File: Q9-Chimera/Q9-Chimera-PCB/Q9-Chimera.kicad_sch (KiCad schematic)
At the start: 199 parts, among them J1 Conn_01x07, J2 USB_C_Receptacle_USB2.0_16P, J3 Conn_01x05, SW1 RotaryEncoder_Switch, SW2 RotaryEncoder_Switch, U1 XC6206PxxxMR, U2 SRV05-4, U3 RP2040, U4 W25Q128JVS, Y1 Crystal_GND24

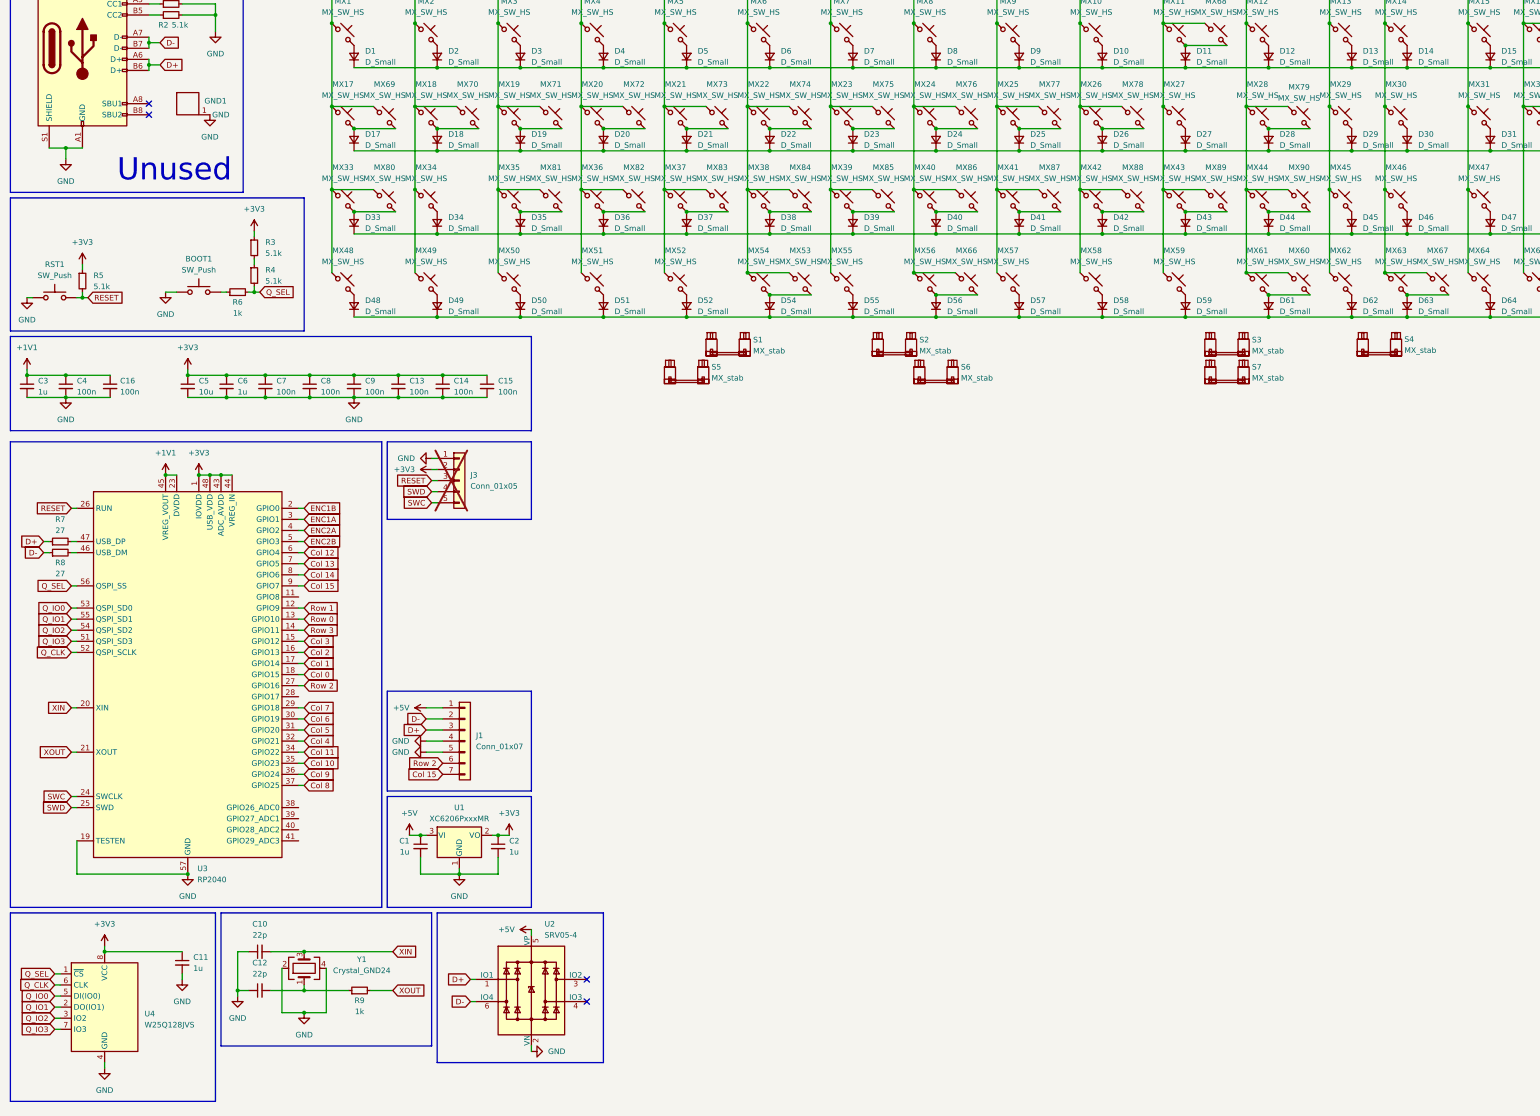
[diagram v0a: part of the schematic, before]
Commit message: complete addition of 225/275 bars and associated tweaks
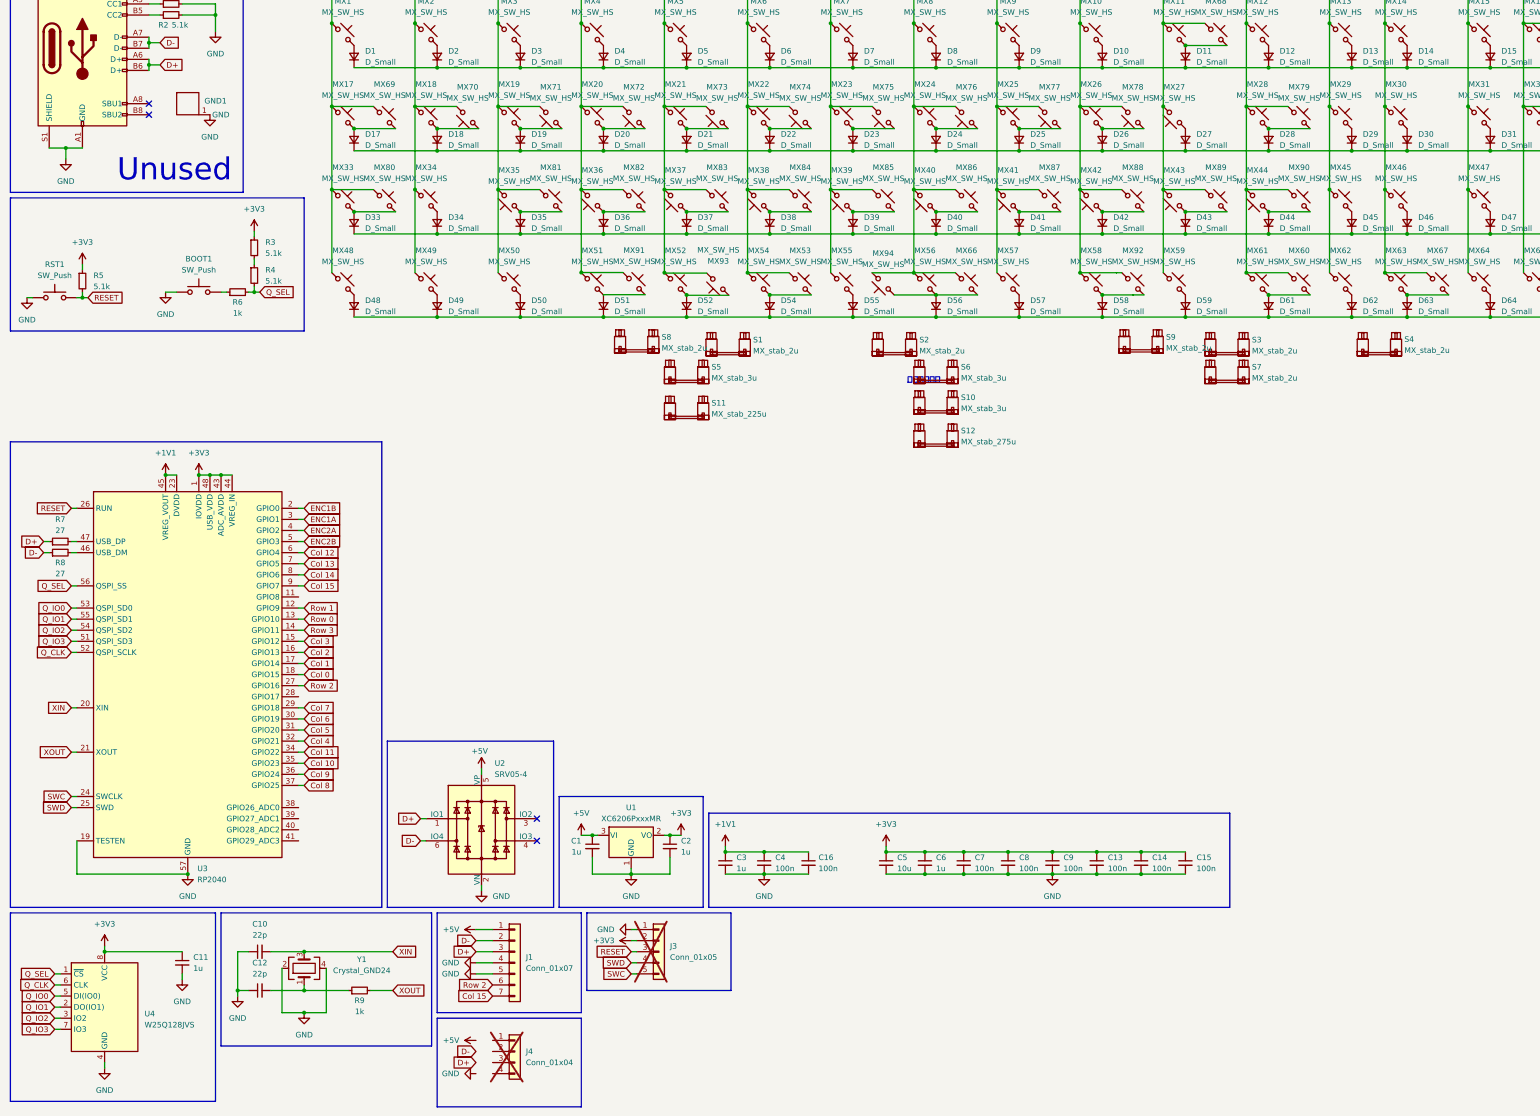
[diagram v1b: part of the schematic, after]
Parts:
- added J4: Conn_01x04, symbol Connector_Generic:Conn_01x04
- added MX91, MX92: MX_SW_HS, PCM_marbastlib-mx:SW_MX_HS_CPG151101S11_1u, symbol PCM_marbastlib-mx:MX_SW_HS_CPG151101S11
- added MX93, MX94: MX_SW_HS, PCM_marbastlib-mx:SW_MX_1u, symbol PCM_marbastlib-mx:MX_SW_HS_CPG151101S11
- added S10: MX_stab_3u, PCM_marbastlib-mx:STAB_MX_3u, symbol PCM_marbastlib-mx:MX_stab
- added S11: MX_stab_225u, PCM_marbastlib-mx:STAB_MX_2.25u, symbol PCM_marbastlib-mx:MX_stab
- added S12: MX_stab_275u, PCM_marbastlib-mx:STAB_MX_2.75u, symbol PCM_marbastlib-mx:MX_stab
- added S8, S9: MX_stab_2u, PCM_marbastlib-mx:STAB_MX_2u, symbol PCM_marbastlib-mx:MX_stab
- MX53: footprint PCM_marbastlib-mx:SW_MX_HS_CPG151101S11_1u -> PCM_marbastlib-mx:SW_MX_1u
- S1, S2, S3, S4, S7: value MX_stab -> MX_stab_2u
- S5, S6: value MX_stab -> MX_stab_3u
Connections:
- net Col 1: now also MX70.2; no longer MX70.1
- net Col 10: now also MX27.2, MX43.2; no longer MX27.1, MX43.1
- net Col 11: now also MX44.2; no longer MX44.1
- net Col 2: now also MX35.2, MX71.2; no longer MX35.1, MX71.1
- net Col 3: now also MX36.2, MX72.2, MX91.1; no longer MX36.1, MX72.1
- net Col 4: now also MX37.2, MX73.2, MX93.2; no longer MX37.1, MX73.1
- net Col 5: now also MX38.2, MX74.2; no longer MX38.1, MX74.1
- net Col 6: now also MX39.2, MX75.2; no longer MX39.1, MX75.1
- net Col 7: now also MX40.2, MX76.2, MX94.2; no longer MX40.1, MX76.1
- net Col 8: now also MX41.2, MX77.2; no longer MX41.1, MX77.1
- net Col 9: now also MX42.2, MX78.2, MX92.1; no longer MX42.1, MX78.1
- net at D39.2 (A), MX85.2: now also MX39.1; no longer MX39.2
- net at D24.2 (A), MX24.2: now also MX76.1; no longer MX76.2
- net at D21.2 (A), MX21.2: now also MX73.1; no longer MX73.2
- net at D40.2 (A), MX86.2: now also MX40.1; no longer MX40.2
- net at D35.2 (A), MX81.2: now also MX35.1; no longer MX35.2
- net at D41.2 (A), MX87.2: now also MX41.1; no longer MX41.2
- net at D20.2 (A), MX20.2: now also MX72.1; no longer MX72.2
- net at D37.2 (A), MX83.2: now also MX37.1; no longer MX37.2
- net at D27.2 (A): now also MX27.1; no longer MX27.2
- net at D22.2 (A), MX22.2: now also MX74.1; no longer MX74.2
- net at D42.2 (A), MX88.2: now also MX42.1; no longer MX42.2
- net at D23.2 (A), MX23.2: now also MX75.1; no longer MX75.2
- net at D18.2 (A), MX18.2: now also MX70.1; no longer MX70.2
- net at D43.2 (A), MX89.2: now also MX43.1; no longer MX43.2
- net at D25.2 (A), MX25.2: now also MX77.1; no longer MX77.2
- net at D58.2 (A), MX58.2: now also MX92.2
- net at D56.2 (A), MX56.2, MX66.2: now also MX94.1
- net at D52.2 (A), MX52.2: now also MX93.1
- net at D51.2 (A), MX51.2: now also MX91.2
- net at D26.2 (A), MX26.2: now also MX78.1; no longer MX78.2
- net at D36.2 (A), MX82.2: now also MX36.1; no longer MX36.2
- net at D44.2 (A), MX90.2: now also MX44.1; no longer MX44.2
- net at D19.2 (A), MX19.2: now also MX71.1; no longer MX71.2
- net at D38.2 (A), MX84.2: now also MX38.1; no longer MX38.2
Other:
- note added: "하수구의제왕"
- moved on the sheet: C1, C13, C14, C15, C16, C2, C3, C4, C5, C6, C7, C8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

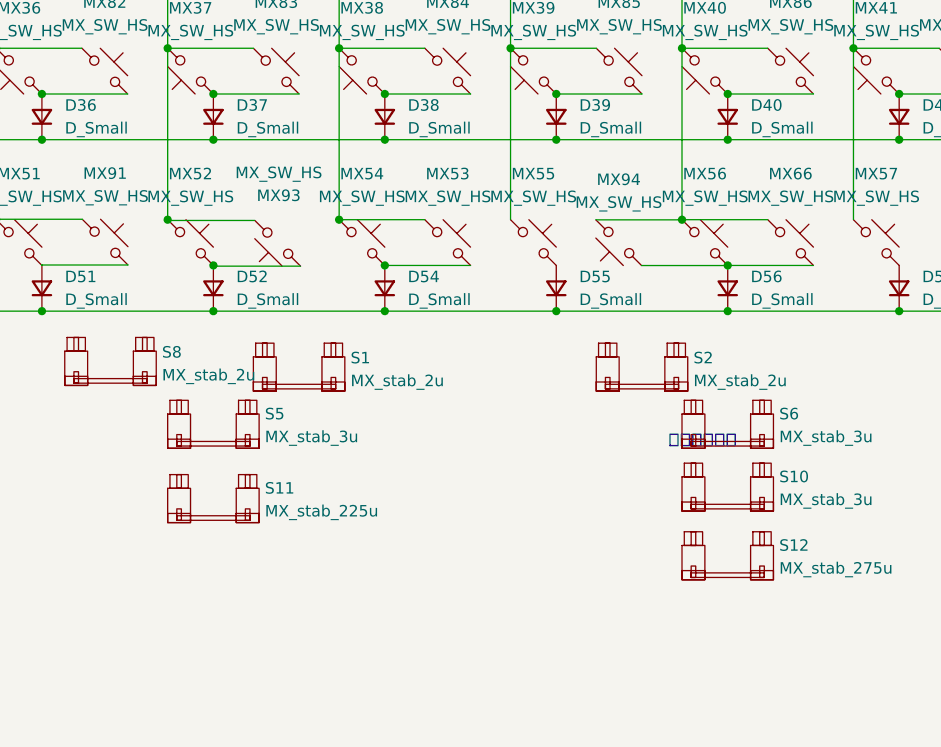
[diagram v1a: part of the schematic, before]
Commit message: split 225/275 to limousine, add 8u/10u support
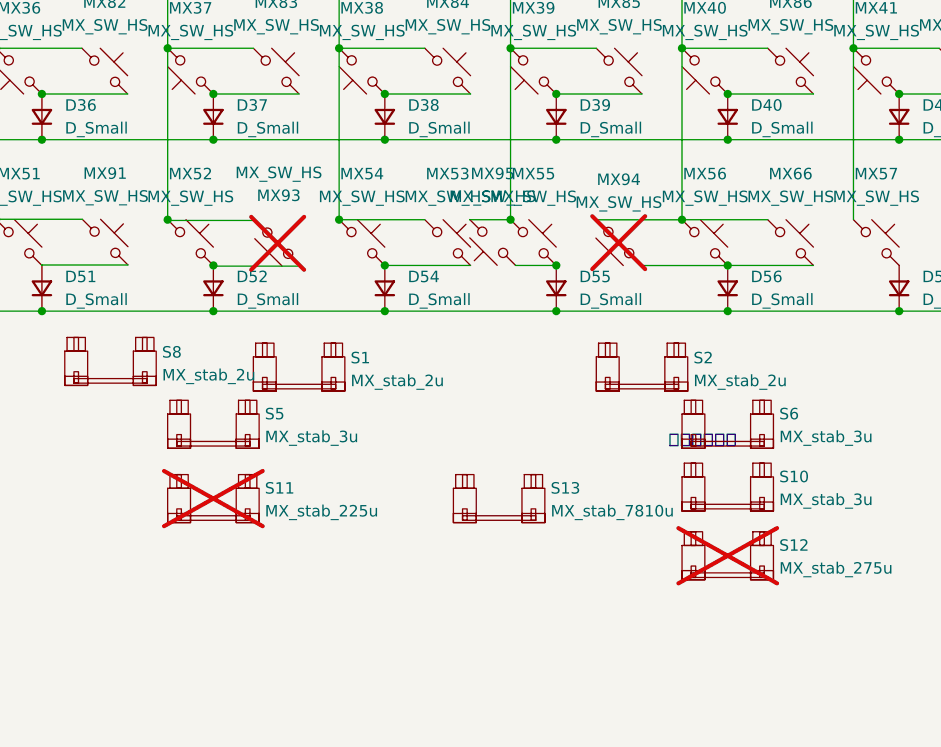
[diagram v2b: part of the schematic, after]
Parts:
- added MX95: MX_SW_HS, PCM_marbastlib-mx:SW_MX_HS_CPG151101S11_1u, symbol PCM_marbastlib-mx:MX_SW_HS_CPG151101S11
- added S13: MX_stab_7810u, PCM_marbastlib-mx:STAB_MX_3u, symbol PCM_marbastlib-mx:MX_stab
- MX53: footprint PCM_marbastlib-mx:SW_MX_1u -> PCM_marbastlib-mx:SW_MX_HS_CPG151101S11_1u
- MX93, MX94, S11, S12: now not fitted; now left out of the parts list
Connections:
- net Col 6: now also MX95.2
- net at D55.2 (A), MX55.2: now also MX95.1
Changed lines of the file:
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@@
 	)
 	(junction
+		(at 207.01 97.155)
+		(diameter 0)
+		(color 0 0 0 0)
+	)
+	(junction
 		(at 262.89 229.87)
 		(diameter 0)
@@
 	)
 	(junction
+		(at 201.93 92.075)
+		(diameter 0)
+		(color 0 0 0 0)
+	)
+	(junction
 		(at 334.01 102.235)
 		(diameter 0)
@@
 	(wire
 		(pts
+			(xy 207.01 97.155) (xy 202.4744 97.155)
+		)
+		(stroke
+			(width 0)
+			(type default)
+		)
+	)
+	(wire
+		(pts
 			(xy 73.66 256.54) (xy 81.28 256.54)
 		)
@@
 	(wire
 		(pts
+			(xy 201.93 92.075) (xy 197.3944 92.075)
+		)
+		(stroke
+			(width 0)
+			(type default)
+		)
+	)
+	(wire
+		(pts
 			(xy 187.96 45.085) (xy 207.01 45.085)
 		)
@@
 	(wire
 		(pts
+			(xy 197.3944 92.075) (xy 197.3944 92.0573)
+		)
+		(stroke
+			(width 0)
+			(type default)
+		)
+	)
+	(wire
+		(pts
 			(xy 245.11 45.085) (xy 264.16 45.085)
 		)
@@
 	(wire
 		(pts
+			(xy 202.4744 97.155) (xy 202.4744 97.1373)
+		)
+		(stroke
+			(width 0)
+			(type default)
+		)
+	)
+	(wire
+		(pts
 			(xy 49.53 96.52) (xy 52.07 96.52)
 		)
@@
 		(unit 1)
 		(exclude_from_sim no)
-		(in_bom yes)
-		(on_board yes)
-		(dnp no)
+		(in_bom no)
+		(on_board no)
+		(dnp yes)
 		(property "Reference" "MX93"
 			(at 176.1749 89.408 0)
@@
 			)
 		)
-		(property "Footprint" "PCM_marbastlib-mx:SW_MX_1u"
+		(property "Footprint" "PCM_marbastlib-mx:SW_MX_HS_CPG151101S11_1u"
 			(at 194.945 94.615 0)
 			(effects
@@
 	)
 	(symbol
+		(lib_id "PCM_marbastlib-mx:MX_stab")
+		(at 200.66 123.19 0)
+		(unit 1)
+		(exclude_from_sim no)
+		(in_bom yes)
+		(on_board yes)
+		(dnp no)
+		(property "Reference" "S13"
+			(at 206.375 121.92 0)
+			(effects
+				(font
+					(size 1.27 1.27)
+				)
+				(justify left)
+			)
+		)
+		(property "Value" "MX_stab_7810u"
+			(at 206.375 124.46 0)
+			(effects
+				(font
+					(size 1.27 1.27)
+				)
+				(justify left)
+			)
+		)
+		(property "Footprint" "PCM_marbastlib-mx:STAB_MX_3u"
+			(at 200.66 123.19 0)
+			(effects
+				(font
+					(size 1.27 1.27)
+				)
+				(hide yes)
+			)
+		)
+		(property "Datasheet" ""
+			(at 200.66 123.19 0)
+			(effects
+				(font
+					(size 1.27 1.27)
+				)
+				(hide yes)
+			)
+		)
+		(property "Description" "Cherry MX-style stabilizer"
+			(at 200.66 123.19 0)
+			(effects
+				(font
+					(size 1.27 1.27)
+				)
+				(hide yes)
+			)
+		)
+		(instances
+			(project "Q9-Chimera"
+				(path "/7ce3128c-8f2e-4572-9e45-99519911b083"
+					(reference "S13")
+					(unit 1)
+				)
+			)
+		)
+	)
+	(symbol
 		(lib_id "PCM_marbastlib-mx:MX_SW_HS_CPG151101S11")
 		(at 350.52 37.465 0)
@@
 	)
 	(symbol
+		(lib_id "PCM_marbastlib-mx:MX_SW_HS_CPG151101S11")
+		(at 199.9344 94.5973 180)
+		(unit 1)
+		(exclude_from_sim no)
+		(in_bom yes)
+		(on_board yes)
+		(dnp no)
+		(fields_autoplaced yes)
+		(property "Reference" "MX95"
+			(at 199.9344 86.9773 0)
+			(effects
+				(font
+					(size 1.27 1.27)
+				)
+			)
+		)
+		(property "Value" "MX_SW_HS"
+			(at 199.9344 89.5173 0)
+			(effects
+				(font
+					(size 1.27 1.27)
+				)
+			)
+		)
+		(property "Footprint" "PCM_marbastlib-mx:SW_MX_HS_CPG151101S11_1u"
+			(at 199.9344 94.5973 0)
+			(effects
+				(font
+					(size 1.27 1.27)
+				)
+				(hide yes)
+			)
+		)
+		(property "Datasheet" "~"
+			(at 199.9344 94.5973 0)
+			(effects
+				(font
+					(size 1.27 1.27)
+				)
+				(hide yes)
+			)
+		)
+		(property "Description" "Push button switch, normally open, two pins, 45° tilted, Kailh CPG151101S11 for Cherry MX style switches"
+			(at 199.9344 94.5973 0)
+			(effects
+				(font
+					(size 1.27 1.27)
+				)
+				(hide yes)
+			)
+		)
+		(pin "2"
+		)
+		(pin "1"
+		)
+		(instances
+			(project "Q9-Chimera"
+				(path "/7ce3128c-8f2e-4572-9e45-99519911b083"
+					(reference "MX95")
+					(unit 1)
+				)
+			)
+		)
+	)
+	(symbol
 		(lib_id "Device:D_Small")
 		(at 187.96 99.695 90)
@@
 		(unit 1)
 		(exclude_from_sim no)
-		(in_bom yes)
-		(on_board yes)
-		(dnp no)
+		(in_bom no)
+		(on_board no)
+		(dnp yes)
 		(property "Reference" "S12"
 			(at 231.775 128.27 0)
@@
 		(unit 1)
 		(exclude_from_sim no)
-		(in_bom yes)
-		(on_board yes)
-		(dnp no)
+		(in_bom no)
+		(on_board no)
+		(dnp yes)
 		(fields_autoplaced yes)
 		(property "Reference" "MX94"
@@
 		(unit 1)
 		(exclude_from_sim no)
-		(in_bom yes)
-		(on_board yes)
-		(dnp no)
+		(in_bom no)
+		(on_board no)
+		(dnp yes)
 		(property "Reference" "S11"
 			(at 174.625 121.92 0)

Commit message: split 225/275 to limousine, add 8u/10u support
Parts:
- S13: footprint PCM_marbastlib-mx:STAB_MX_3u -> PCM_marbastlib-mx:STAB_MX_10u
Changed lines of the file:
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@@
 			)
 		)
-		(property "Footprint" "PCM_marbastlib-mx:STAB_MX_3u"
+		(property "Footprint" "PCM_marbastlib-mx:STAB_MX_10u"
 			(at 200.66 123.19 0)
 			(effects

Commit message: prep v1.1 release
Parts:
- J1: LCSC Part # (none) -> C160393
- MX53, MX60, MX95: footprint PCM_marbastlib-mx:SW_MX_HS_CPG151101S11_1u -> PCM_marbastlib-mx:SW_MX_1u
- U1: LCSC Part # (none) -> C2897477
- U2: LCSC Part # (none) -> C2836319
- U3: LCSC Part # (none) -> C2040
- U4: LCSC Part # (none) -> C97521
- Y1: LCSC Part # (none) -> C403945
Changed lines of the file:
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@@
 			)
 		)
-		(property "Footprint" "PCM_marbastlib-mx:SW_MX_HS_CPG151101S11_1u"
+		(property "Footprint" "PCM_marbastlib-mx:SW_MX_1u"
 			(at 194.945 94.615 0)
 			(effects
@@
 			)
 		)
+		(property "LCSC Part #" "C2836319"
+			(at 121.92 219.71 0)
+			(effects
+				(font
+					(size 1.27 1.27)
+				)
+				(hide yes)
+			)
+		)
 		(pin "4"
 		)
@@
 			)
 		)
+		(property "LCSC Part #" "C97521"
+			(at 35.56 260.35 0)
+			(effects
+				(font
+					(size 1.27 1.27)
+				)
+				(hide yes)
+			)
+		)
 		(pin "1"
 		)
@@
 			)
 		)
-		(property "Footprint" "PCM_marbastlib-mx:SW_MX_HS_CPG151101S11_1u"
+		(property "Footprint" "PCM_marbastlib-mx:SW_MX_1u"
 			(at 309.245 94.615 0)
 			(effects
@@
 			)
 		)
+		(property "LCSC Part #" "C2897477"
+			(at 156.21 220.98 0)
+			(effects
+				(font
+					(size 1.27 1.27)
+				)
+				(hide yes)
+			)
+		)
 		(pin "3"
 		)
@@
 			)
 		)
-		(property "Footprint" "PCM_marbastlib-mx:SW_MX_HS_CPG151101S11_1u"
+		(property "Footprint" "PCM_marbastlib-mx:SW_MX_1u"
 			(at 199.9344 94.5973 0)
 			(effects
@@
 			)
 		)
+		(property "LCSC Part #" "C160393"
+			(at 129.54 250.19 0)
+			(effects
+				(font
+					(size 1.27 1.27)
+				)
+				(hide yes)
+			)
+		)
 		(pin "5"
 		)
@@
 			)
 		)
+		(property "LCSC Part #" "C2040"
+			(at 54.61 184.15 0)
+			(effects
+				(font
+					(size 1.27 1.27)
+				)
+				(hide yes)
+			)
+		)
 		(pin "35"
 		)
@@
 			(effects
 				(font
+					(size 1.27 1.27)
+				)
+				(hide yes)
+			)
+		)
+		(property "LCSC Part #" "C403945"
+			(at 81.28 251.46 90)
+			(effects
+				(font
